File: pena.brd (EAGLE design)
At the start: 93.8 x 80.1 mm, 35 parts

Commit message: Vaihdettu boardin kokoa.
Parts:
- moved JP7 11.7 mm to (64.1, 65.4)
- moved CS 11.7 mm to (70.5, 38.8)
- moved GND 11.7 mm to (73.5, 35.8)
- moved JP1 11.7 mm to (62.8, 76.9)
- moved JP3 11.7 mm to (64.1, 45.1)
- moved R1 11.7 mm to (9.39, 74.1)
- moved R10 11.7 mm to (23.6, 40.8)
- moved R2 11.7 mm to (23.1, 74.3)
- moved R6 11.7 mm to (23.6, 57.3)
- moved S1 11.7 mm to (9.20, 74.1)
- moved S2 11.7 mm to (23.2, 74.1)
- moved S3 11.7 mm to (37.8, 74.1)
- moved S4 11.7 mm to (52.4, 74.1)
- moved SI 11.7 mm to (70.5, 41.7)
- moved VCC 11.7 mm to (70.5, 35.8)
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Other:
- board size 93.8 x 80.1 mm -> 82.2 x 59.3 mm

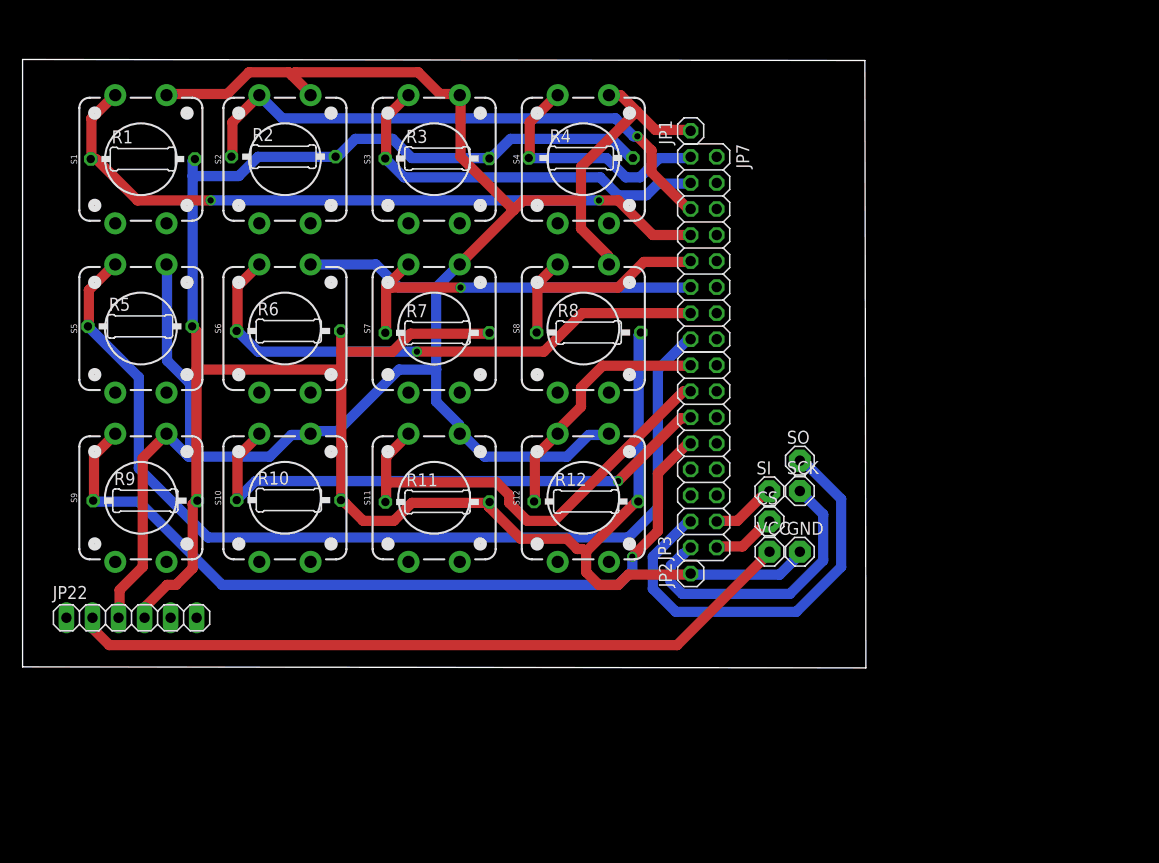
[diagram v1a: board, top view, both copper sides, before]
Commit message: Muutettu boardin kokoa, reikien kokoa sekä poistettu alasveto vastukset.
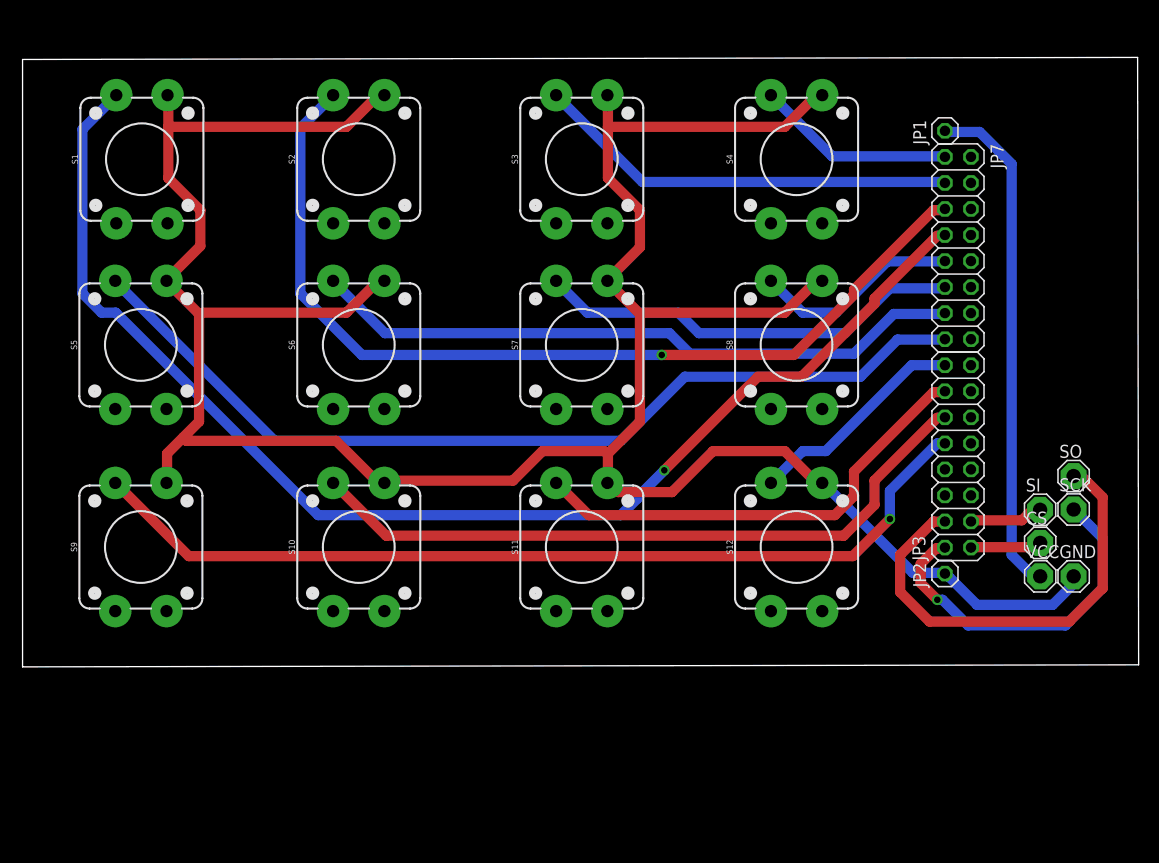
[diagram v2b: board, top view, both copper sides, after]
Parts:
- removed JP22: (no value), mega:1X06
- removed R1, R10, R11, R12, R2, R3, R4, R5, R6, R7, R8, R9: (no value), resistor:0207/10
- CS, GND, SCK, SI, SO, VCC: value MCS10B -> SE14; device solpad:MCS10B -> solpad:SE14
- JP3: device mega:2X08 -> pinhead:2X08
- JP7: device pena:2X08 -> pinhead:2X08
- S1, S10, S11, S12, S2, S3, S4, S5, S6, S7, S8, S9: device mega:TACTILE_SWITCH_PTH_12MM -> SparkFun-Switches:TACTILE_SWITCH_PTH_12MM
- moved GND 26.8 mm to (100.2, 33.4)
- moved SCK 26.8 mm to (100.2, 39.9)
- moved SO 26.7 mm to (100.2, 43.2)
- moved VCC 26.5 mm to (96.9, 33.4)
- moved CS 26.5 mm to (96.9, 36.7)
- moved SI 26.5 mm to (96.9, 39.9)
- moved JP1 24.8 mm to (87.6, 76.9)
- moved JP2 24.8 mm to (87.6, 33.7)
- moved JP3 24.8 mm to (88.9, 45.1)
- moved JP7 24.8 mm to (88.9, 65.4)
- moved S12 21.3 mm to (73.2, 36.3)
- moved S8 20.9 mm to (73.2, 56.0)
- moved S4 20.8 mm to (73.2, 74.1)
- moved S11 15.2 mm to (52.2, 36.3)
- moved S7 14.5 mm to (52.2, 56.0)
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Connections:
- removed net +3V: JP22.2, VCC.MP
- net +5V: now also VCC.MP; no longer JP22.3, S1.1, S10.1, S11.1, S12.1, S2.1, S3.1, S4.1, S5.1, S6.1, S7.1, S8.1, S9.1
- net 22: no longer R4.1
- net 24: no longer R3.1
- net 26: no longer R2.1
- net 28: no longer R1.1
- net 30: no longer R8.1
- net 32: no longer R7.1
- net 34: no longer R6.1
- net 36: no longer R5.1
- net 38: no longer R12.1
- net 40: no longer R11.1
- net 42: no longer R10.1
- net 44: no longer R9.1
- net GND: now also S1.1, S10.1, S11.1, S12.1, S2.1, S3.1, S4.1, S5.1, S6.1, S7.1, S8.1, S9.1; no longer JP22.4, R1.2, R10.2, R11.2, R12.2, R2.2, R3.2, R4.2, R5.2, R6.2, R7.2, R8.2, R9.2
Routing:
- net +5V: track 207.4 -> 49.7 mm
- net +3V: track 71.6 -> 0.00 mm
- net 28: track 68.8 -> 125.5 mm, vias 2 -> 1
- net GND: track 217.0 -> 269.1 mm
- net 26: track 55.0 -> 92.2 mm
- net 42: track 55.0 -> 68.0 mm, vias 1 -> 0
- net 44: track 78.9 -> 90.0 mm
- net 34: track 54.1 -> 64.3 mm, vias 1 -> 0
- net 52: track 28.7 -> 34.7 mm, vias 0 -> 1
- net 22: track 24.8 -> 19.5 mm
- net 32: track 37.3 -> 41.9 mm, vias 1 -> 0
- net 36: track 95.6 -> 91.5 mm
- net 30: track 23.6 -> 20.3 mm
- net 38: track 24.5 -> 21.7 mm
- net 50: track 41.6 -> 44.2 mm
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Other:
- board size 82.2 x 59.3 mm -> 108.9 x 59.4 mm

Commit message: Muutettu boardin kokoa sekä jarjestelty nappeja.
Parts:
- moved S12 4.74 mm to (77.7, 34.8)
- moved S8 4.65 mm to (77.3, 54.0)
- moved S4 4.13 mm to (77.2, 73.6)
- moved S7 4.03 mm to (55.7, 54.0)
- moved S11 3.81 mm to (55.7, 34.8)
- moved S6 3.61 mm to (33.5, 54.0)
- moved S3 3.50 mm to (55.7, 74.1)
- moved S10 3.35 mm to (33.5, 34.8)
- moved S2 3.00 mm to (33.5, 74.1)
- moved S5 2.50 mm to (9.20, 53.5)
- moved JP1 1.50 mm to (89.1, 76.9)
- moved JP2 1.50 mm to (89.1, 33.7)
- moved JP3 1.50 mm to (90.4, 45.1)
- moved JP7 1.50 mm to (90.4, 65.4)
- moved S9 1.50 mm to (9.20, 34.8)
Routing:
- net 28: track 125.5 -> 90.0 mm
- net 26: track 92.2 -> 62.8 mm
- net GND: track 269.1 -> 286.8 mm
- net 42: track 68.0 -> 61.6 mm, vias 0 -> 1
- net 36: track 91.5 -> 85.5 mm
- net 30: track 20.3 -> 15.9 mm
- net 52: track 34.7 -> 31.8 mm, vias 1 -> 0
- net 22: track 19.5 -> 16.7 mm
- net 32: track 41.9 -> 39.3 mm
- net 40: track 45.6 -> 43.0 mm
- net 24: track 41.5 -> 39.5 mm
- net 53: track 6.93 -> 5.43 mm
- net 51: track 7.22 -> 5.78 mm
- net 50: track 44.2 -> 43.1 mm, vias 0 -> 1
- net 38: track 21.7 -> 20.7 mm
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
